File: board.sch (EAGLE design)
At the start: 6 parts

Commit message: minor updates
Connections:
- new net GND: PORTD.7, PORTD.8, U$1.GND
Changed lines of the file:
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@@
 <part name="PORTB" library="SparkFun-Connectors" deviceset="M04" device="PTH"/>
 <part name="PORTE" library="SparkFun-Connectors" deviceset="M04" device="PTH"/>
+<part name="GND1" library="supply1" deviceset="GND" device=""/>
+<part name="GND2" library="supply1" deviceset="GND" device=""/>
 </parts>
 <sheets>
@@
 <instance part="PORTB" gate="G$1" x="99.06" y="101.6"/>
 <instance part="PORTE" gate="G$1" x="99.06" y="83.82"/>
+<instance part="GND1" gate="1" x="78.74" y="109.22" rot="R180"/>
+<instance part="GND2" gate="1" x="48.26" y="30.48"/>
 </instances>
 <busses>
 </busses>
 <nets>
+<net name="GND" class="0">
+<segment>
+<pinref part="PORTD" gate="G$1" pin="7"/>
+<pinref part="PORTD" gate="G$1" pin="8"/>
+<wire x1="78.74" y1="104.14" x2="78.74" y2="106.68" width="0.1524" layer="91"/>
+<pinref part="GND1" gate="1" pin="GND"/>
+<junction x="78.74" y="106.68"/>
+</segment>
+<segment>
+<pinref part="U$1" gate="G$1" pin="GND"/>
+<pinref part="GND2" gate="1" pin="GND"/>
+</segment>
+</net>
 </nets>
 </sheet>

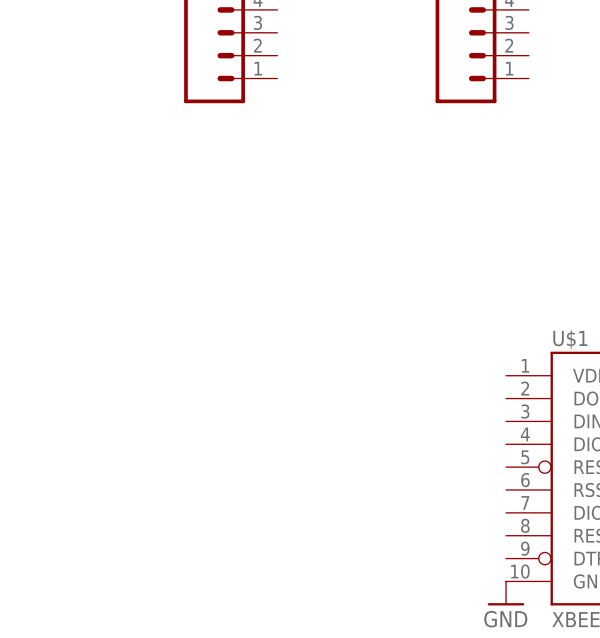
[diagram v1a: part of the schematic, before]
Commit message: placing a stacking header so we can get reset and 3.3v from the xmega board
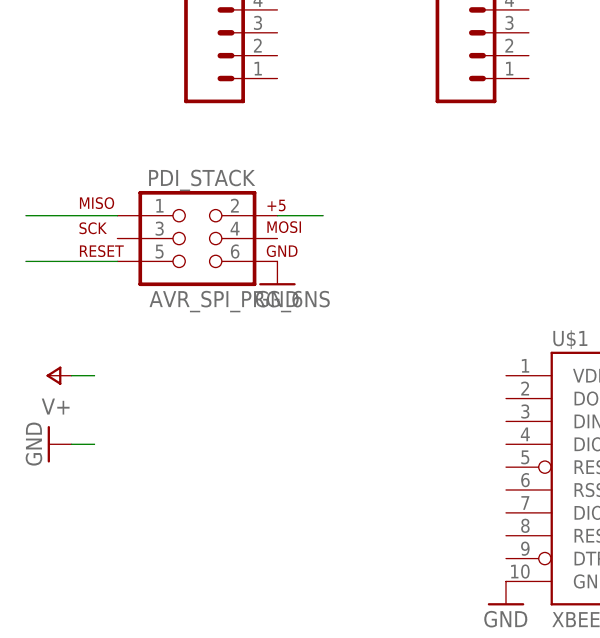
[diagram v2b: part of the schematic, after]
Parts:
- added PDI_STACK: AVR_SPI_PRG_6NS, SparkFun-Connectors:AVR_SPI_PRG_6NS
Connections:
- new net PDI_DATA: PDI_STACK.1
- new net PDI_RESET/CLK: PDI_STACK.5
- new net VXMEGA: PDI_STACK.2
- net GND: now also PDI_STACK.6
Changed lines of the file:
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@@
 <part name="GND1" library="supply1" deviceset="GND" device=""/>
 <part name="GND2" library="supply1" deviceset="GND" device=""/>
+<part name="PDI_STACK" library="SparkFun-Connectors" deviceset="AVR_SPI_PRG_6" device="NS"/>
+<part name="P+1" library="supply1" deviceset="V+" device=""/>
+<part name="GND3" library="supply1" deviceset="GND" device=""/>
+<part name="GND4" library="supply1" deviceset="GND" device=""/>
 </parts>
 <sheets>
@@
 <instance part="GND1" gate="1" x="78.74" y="109.22" rot="R180"/>
 <instance part="GND2" gate="1" x="48.26" y="30.48"/>
+<instance part="PDI_STACK" gate="G$1" x="12.7" y="71.12"/>
+<instance part="P+1" gate="1" x="-2.54" y="55.88" rot="R90"/>
+<instance part="GND3" gate="1" x="-2.54" y="48.26" rot="R270"/>
+<instance part="GND4" gate="1" x="22.86" y="66.04"/>
 </instances>
 <busses>
@@
 <pinref part="GND2" gate="1" pin="GND"/>
 </segment>
+<segment>
+<pinref part="GND3" gate="1" pin="GND"/>
+<wire x1="0" y1="48.26" x2="2.54" y2="48.26" width="0.1524" layer="91"/>
+</segment>
+<segment>
+<pinref part="PDI_STACK" gate="G$1" pin="6"/>
+<pinref part="GND4" gate="1" pin="GND"/>
+</segment>
 </net>
+<net name="VBAT" class="0">
+<segment>
+<pinref part="P+1" gate="1" pin="V+"/>
+<wire x1="0" y1="55.88" x2="2.54" y2="55.88" width="0.1524" layer="91"/>
+</segment>
+</net>
+<net name="PDI_DATA" class="0">
+<segment>
+<pinref part="PDI_STACK" gate="G$1" pin="1"/>
+<wire x1="5.08" y1="73.66" x2="-5.08" y2="73.66" width="0.1524" layer="91"/>
+</segment>
+</net>
+<net name="PDI_RESET/CLK" class="0">
+<segment>
+<pinref part="PDI_STACK" gate="G$1" pin="5"/>
+<wire x1="5.08" y1="68.58" x2="-5.08" y2="68.58" width="0.1524" layer="91"/>
+</segment>
+</net>
+<net name="VXMEGA" class="0">
+<segment>
+<pinref part="PDI_STACK" gate="G$1" pin="2"/>
+<wire x1="22.86" y1="73.66" x2="27.94" y2="73.66" width="0.1524" layer="91"/>
+</segment>
+</net>

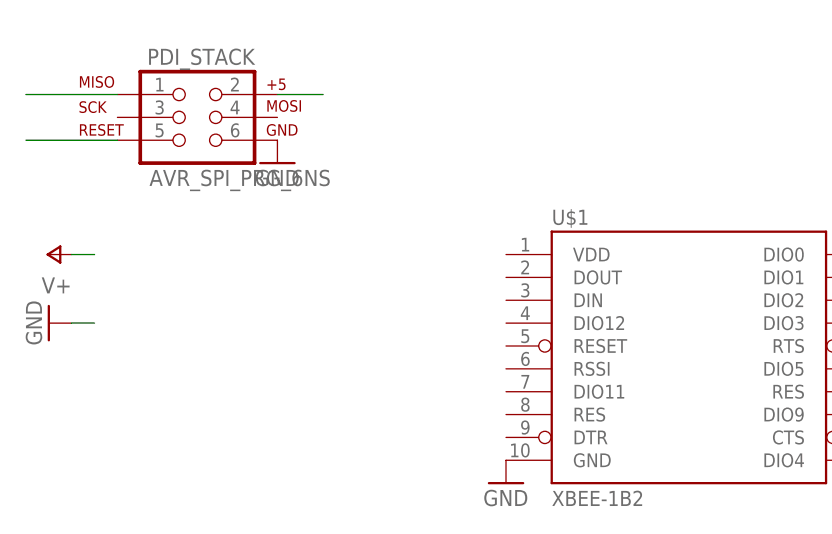
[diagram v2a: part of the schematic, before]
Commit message: stack the power connector too and mark out the 50x50mm board area for cheapest chinese boards
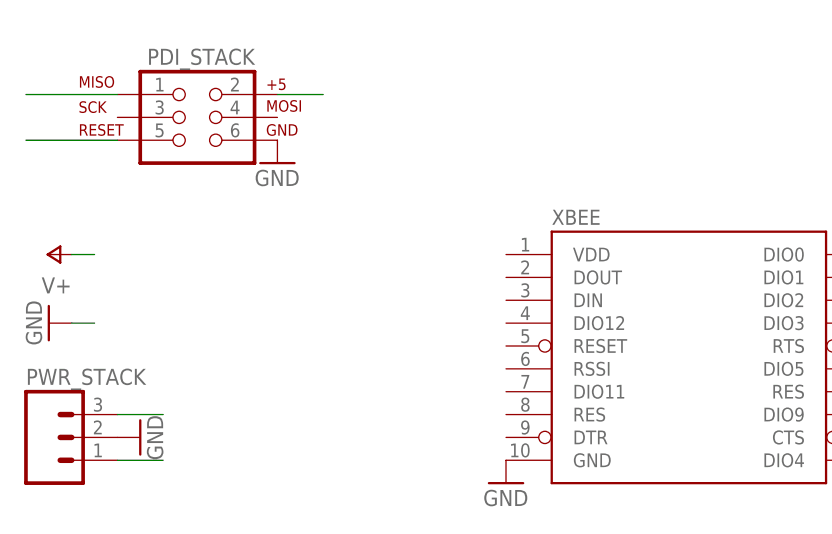
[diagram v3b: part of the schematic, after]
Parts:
- added PWR_STACK: (no value), SparkFun-Connectors:M03PTH
- renumbered U$1 to XBEE
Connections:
- new net VBAT: PWR_STACK.1
- net GND: now also PWR_STACK.2
- net VXMEGA: now also PWR_STACK.3
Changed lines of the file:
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@@
 </classes>
 <parts>
-<part name="U$1" library="SparkFun-RF" deviceset="XBEE-1" device="B2"/>
+<part name="XBEE" library="SparkFun-RF" deviceset="XBEE-1" device="B2"/>
 <part name="PORTA" library="SparkFun-Connectors" deviceset="M08" device="1X08"/>
 <part name="PORTC" library="SparkFun-Connectors" deviceset="M08" device="1X08"/>
@@
 <part name="GND3" library="supply1" deviceset="GND" device=""/>
 <part name="GND4" library="supply1" deviceset="GND" device=""/>
+<part name="PWR_STACK" library="SparkFun-Connectors" deviceset="M03" device="PTH"/>
+<part name="GND5" library="supply1" deviceset="GND" device=""/>
 </parts>
 <sheets>
@@
 </plain>
 <instances>
-<instance part="U$1" gate="G$1" x="68.58" y="45.72"/>
+<instance part="XBEE" gate="G$1" x="68.58" y="45.72" smashed="yes">
+<attribute name="NAME" x="53.34" y="59.182" size="1.6764" layer="95"/>
+</instance>
 <instance part="PORTA" gate="G$1" x="17.78" y="96.52"/>
 <instance part="PORTC" gate="G$1" x="45.72" y="96.52"/>
@@
 <instance part="GND1" gate="1" x="78.74" y="109.22" rot="R180"/>
 <instance part="GND2" gate="1" x="48.26" y="30.48"/>
-<instance part="PDI_STACK" gate="G$1" x="12.7" y="71.12"/>
+<instance part="PDI_STACK" gate="G$1" x="12.7" y="71.12" smashed="yes">
+<attribute name="NAME" x="8.382" y="76.962" size="1.778" layer="95"/>
+</instance>
 <instance part="P+1" gate="1" x="-2.54" y="55.88" rot="R90"/>
 <instance part="GND3" gate="1" x="-2.54" y="48.26" rot="R270"/>
 <instance part="GND4" gate="1" x="22.86" y="66.04"/>
+<instance part="PWR_STACK" gate="G$1" x="-2.54" y="35.56"/>
+<instance part="GND5" gate="1" x="7.62" y="35.56" rot="R90"/>
 </instances>
 <busses>
@@
 </segment>
 <segment>
-<pinref part="U$1" gate="G$1" pin="GND"/>
+<pinref part="XBEE" gate="G$1" pin="GND"/>
 <pinref part="GND2" gate="1" pin="GND"/>
 </segment>
@@
 <pinref part="GND4" gate="1" pin="GND"/>
 </segment>
+<segment>
+<pinref part="PWR_STACK" gate="G$1" pin="2"/>
+<pinref part="GND5" gate="1" pin="GND"/>
+</segment>
 </net>
 <net name="VBAT" class="0">
@@
 <pinref part="P+1" gate="1" pin="V+"/>
 <wire x1="0" y1="55.88" x2="2.54" y2="55.88" width="0.1524" layer="91"/>
+</segment>
+<segment>
+<pinref part="PWR_STACK" gate="G$1" pin="1"/>
+<wire x1="5.08" y1="33.02" x2="10.16" y2="33.02" width="0.1524" layer="91"/>
 </segment>
 </net>
@@
 <wire x1="22.86" y1="73.66" x2="27.94" y2="73.66" width="0.1524" layer="91"/>
 </segment>
+<segment>
+<pinref part="PWR_STACK" gate="G$1" pin="3"/>
+<wire x1="5.08" y1="38.1" x2="10.16" y2="38.1" width="0.1524" layer="91"/>
+</segment>
 </net>

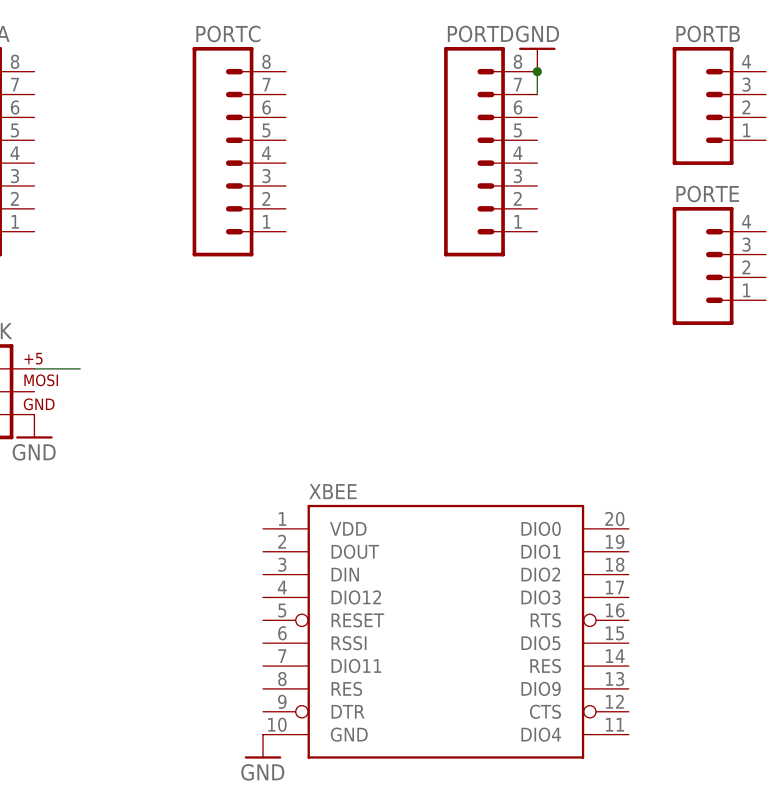
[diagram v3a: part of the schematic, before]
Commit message: use the stub portd for rx/tx in case someone is using the rtc xtal on porte
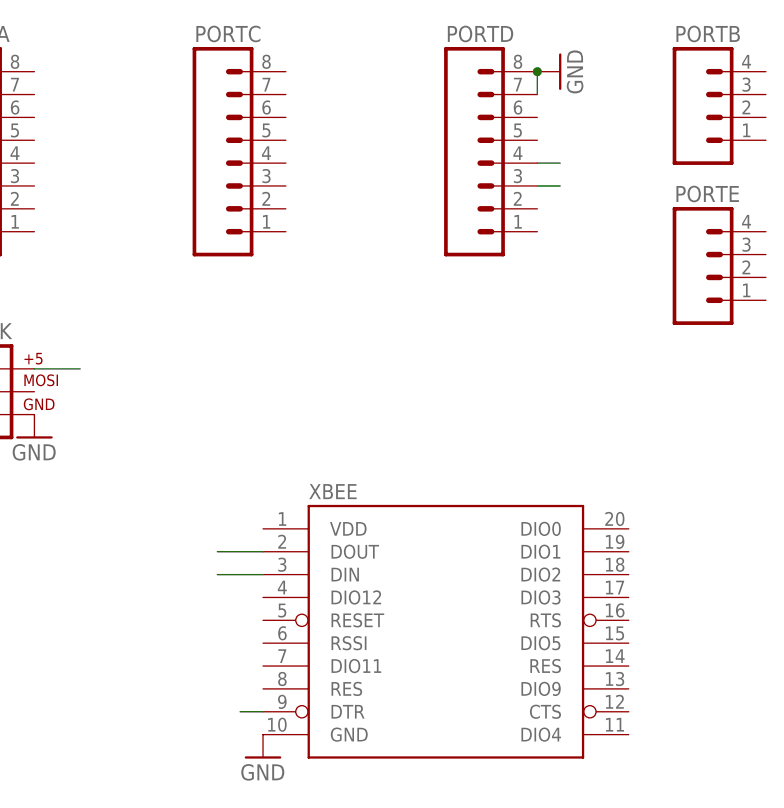
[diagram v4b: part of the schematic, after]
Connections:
- new net XMEGA_RX: PORTD.3, XBEE.DOUT
- new net XMEGA_TX: PORTD.4, XBEE.DIN
- net PDI_RESET/CLK: now also XBEE.DTR
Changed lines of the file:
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@@
 <instance part="PORTB" gate="G$1" x="99.06" y="101.6"/>
 <instance part="PORTE" gate="G$1" x="99.06" y="83.82"/>
-<instance part="GND1" gate="1" x="78.74" y="109.22" rot="R180"/>
+<instance part="GND1" gate="1" x="81.28" y="106.68" rot="R90"/>
 <instance part="GND2" gate="1" x="48.26" y="30.48"/>
 <instance part="PDI_STACK" gate="G$1" x="12.7" y="71.12" smashed="yes">
@@
 <wire x1="5.08" y1="68.58" x2="-5.08" y2="68.58" width="0.1524" layer="91"/>
 </segment>
+<segment>
+<pinref part="XBEE" gate="G$1" pin="DTR"/>
+<wire x1="48.26" y1="35.56" x2="45.72" y2="35.56" width="0.1524" layer="91"/>
+</segment>
 </net>
 <net name="VXMEGA" class="0">
@@
 </segment>
 </net>
+<net name="XMEGA_RX" class="0">
+<segment>
+<pinref part="PORTD" gate="G$1" pin="3"/>
+<wire x1="78.74" y1="93.98" x2="81.28" y2="93.98" width="0.1524" layer="91"/>
+</segment>
+<segment>
+<pinref part="XBEE" gate="G$1" pin="DOUT"/>
+<wire x1="48.26" y1="53.34" x2="43.18" y2="53.34" width="0.1524" layer="91"/>
+</segment>
+</net>
+<net name="XMEGA_TX" class="0">
+<segment>
+<pinref part="PORTD" gate="G$1" pin="4"/>
+<wire x1="78.74" y1="96.52" x2="81.28" y2="96.52" width="0.1524" layer="91"/>
+</segment>
+<segment>
+<pinref part="XBEE" gate="G$1" pin="DIN"/>
+<wire x1="48.26" y1="50.8" x2="43.18" y2="50.8" width="0.1524" layer="91"/>
+</segment>
+</net>

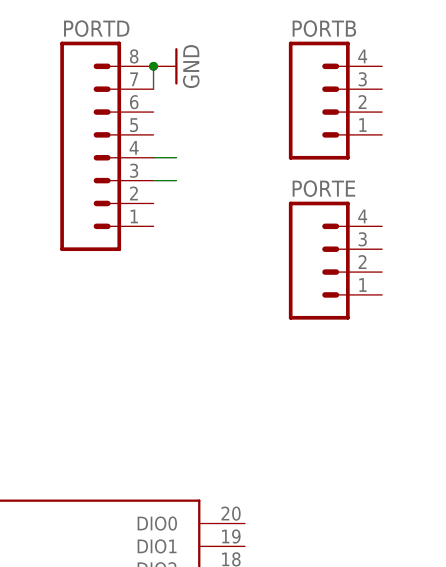
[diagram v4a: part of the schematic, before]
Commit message: use the stub portd for rx/tx in case someone is using the rtc xtal on porte
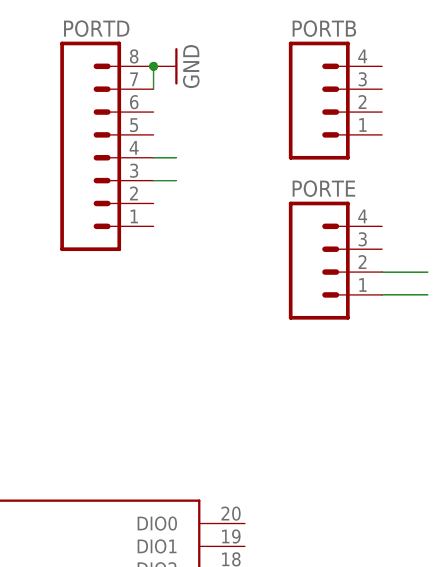
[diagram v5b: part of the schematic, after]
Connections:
- new net SCL: PORTE.2
- new net SDA: PORTE.1
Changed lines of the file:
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@@
+</segment>
+</net>
+<net name="SDA" class="0">
+<segment>
+<pinref part="PORTE" gate="G$1" pin="1"/>
+<wire x1="104.14" y1="81.28" x2="109.22" y2="81.28" width="0.1524" layer="91"/>
+</segment>
+</net>
+<net name="SCL" class="0">
+<segment>
+<pinref part="PORTE" gate="G$1" pin="2"/>
+<wire x1="104.14" y1="83.82" x2="109.22" y2="83.82" width="0.1524" layer="91"/>
 </segment>
 </net>

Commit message: noted the second UART
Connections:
- net VBAT renamed VXMEGA_USB
- net XMEGA_RX renamed XMEGA_RX0
- net XMEGA_TX renamed XMEGA_TX0
- new net XMEGA_RX1: PORTC.7
- new net XMEGA_TX1: PORTC.8
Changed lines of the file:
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@@
 <wire x1="0" y1="55.88" x2="2.54" y2="55.88" width="0.1524" layer="91"/>
-</segment>
-<segment>
-<pinref part="PWR_STACK" gate="G$1" pin="1"/>
-<wire x1="5.08" y1="33.02" x2="10.16" y2="33.02" width="0.1524" layer="91"/>
 </segment>
 </net>
@@
 </segment>
 </net>
-<net name="XMEGA_RX" class="0">
+<net name="XMEGA_RX0" class="0">
 <segment>
 <pinref part="PORTD" gate="G$1" pin="3"/>
@@
 </segment>
 </net>
-<net name="XMEGA_TX" class="0">
+<net name="XMEGA_TX0" class="0">
 <segment>
 <pinref part="PORTD" gate="G$1" pin="4"/>
@@
 </segment>
 </net>
+<net name="VXMEGA_USB" class="0">
+<segment>
+<pinref part="PWR_STACK" gate="G$1" pin="1"/>
+<wire x1="5.08" y1="33.02" x2="10.16" y2="33.02" width="0.1524" layer="91"/>
+</segment>
+</net>
+<net name="XMEGA_TX1" class="0">
+<segment>
+<pinref part="PORTC" gate="G$1" pin="8"/>
+<wire x1="50.8" y1="106.68" x2="53.34" y2="106.68" width="0.1524" layer="91"/>
+</segment>
+</net>
+<net name="XMEGA_RX1" class="0">
+<segment>
+<pinref part="PORTC" gate="G$1" pin="7"/>
+<wire x1="50.8" y1="104.14" x2="53.34" y2="104.14" width="0.1524" layer="91"/>
+</segment>
+</net>
